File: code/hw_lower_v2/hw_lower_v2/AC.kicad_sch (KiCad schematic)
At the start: 38 parts, among them K1 AHES4191, Q1 BSS138, Q2 BSS138, Q3 BSS138, T1 TS3193-2C 2mA/2mA, U1 BRCS02C, U2 BL0942

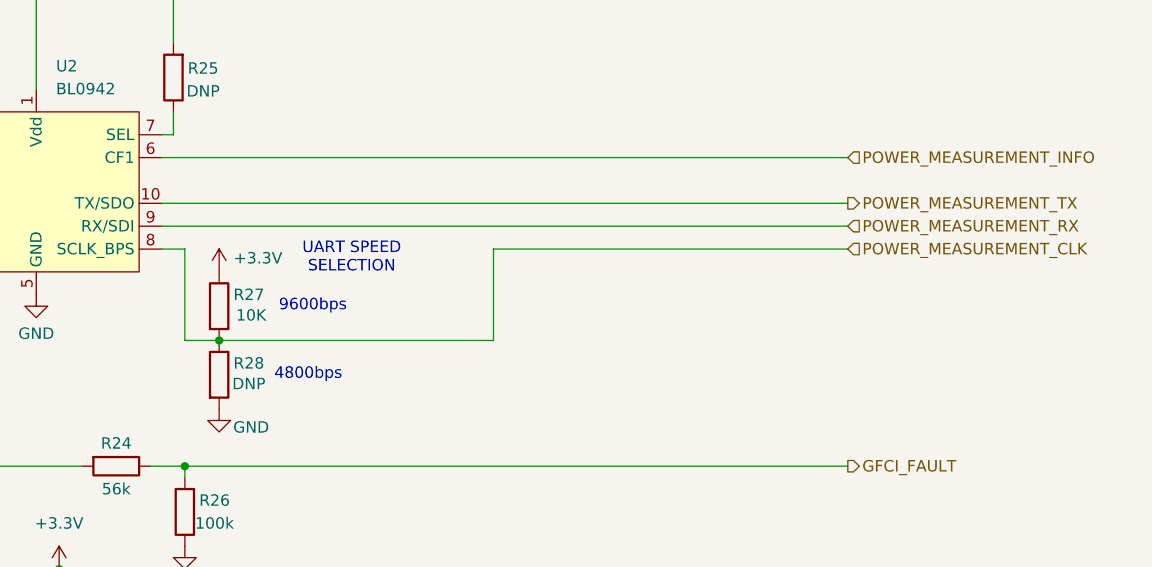
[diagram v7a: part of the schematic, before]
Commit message: grouped and positioned components
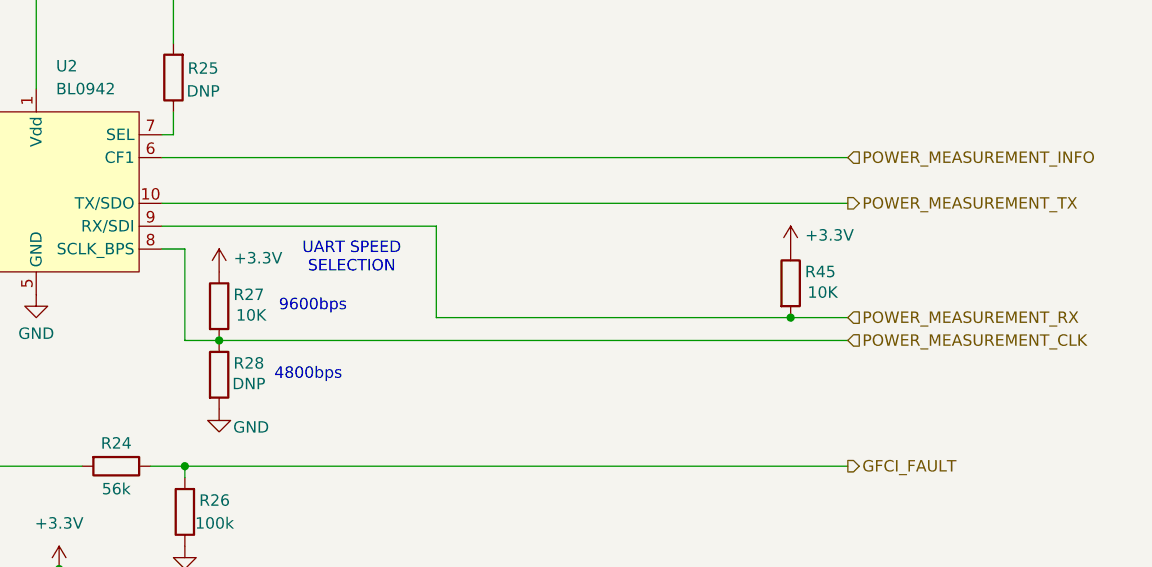
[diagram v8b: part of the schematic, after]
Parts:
- added R45: 10K, Resistor_SMD:R_0603_1608Metric, symbol Device:R
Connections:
- net +3.3V: now also R45.1
- net POWER_MEASUREMENT_RX: now also R45.2
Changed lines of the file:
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@@
 	)
 	(junction
+		(at 240.03 69.85)
+		(diameter 0)
+		(color 0 0 0 0)
+	)
+	(junction
 		(at 97.79 49.53)
 		(diameter 0)
@@
 	(wire
 		(pts
+			(xy 200.66 69.85) (xy 200.66 59.69)
+		)
+		(stroke
+			(width 0)
+			(type default)
+		)
+	)
+	(wire
+		(pts
 			(xy 147.32 33.02) (xy 156.21 33.02)
 		)
@@
 	(wire
 		(pts
-			(xy 170.18 59.69) (xy 246.38 59.69)
+			(xy 240.03 69.85) (xy 246.38 69.85)
+		)
+		(stroke
+			(width 0)
+			(type default)
+		)
+	)
+	(wire
+		(pts
+			(xy 200.66 69.85) (xy 240.03 69.85)
 		)
 		(stroke
@@
 	(wire
 		(pts
-			(xy 207.01 72.39) (xy 207.01 62.23)
+			(xy 109.22 49.53) (xy 146.05 49.53)
 		)
 		(stroke
@@
 	(wire
 		(pts
-			(xy 109.22 49.53) (xy 146.05 49.53)
+			(xy 29.21 77.47) (xy 29.21 83.82)
 		)
 		(stroke
@@
 	(wire
 		(pts
-			(xy 29.21 77.47) (xy 29.21 83.82)
+			(xy 116.84 67.31) (xy 101.6 67.31)
 		)
 		(stroke
@@
 	(wire
 		(pts
-			(xy 116.84 67.31) (xy 101.6 67.31)
+			(xy 200.66 59.69) (xy 170.18 59.69)
 		)
 		(stroke
@@
 	(wire
 		(pts
-			(xy 207.01 62.23) (xy 246.38 62.23)
-		)
-		(stroke
-			(width 0)
-			(type default)
-		)
-	)
-	(wire
-		(pts
 			(xy 101.6 137.16) (xy 107.95 137.16)
 		)
@@
 	(wire
 		(pts
-			(xy 176.53 72.39) (xy 207.01 72.39)
+			(xy 176.53 72.39) (xy 246.38 72.39)
 		)
 		(stroke
@@
 	(hierarchical_label "POWER_MEASUREMENT_RX"
 		(shape input)
-		(at 246.38 59.69 0)
+		(at 246.38 69.85 0)
 		(fields_autoplaced yes)
 		(effects
@@
 	(hierarchical_label "POWER_MEASUREMENT_CLK"
 		(shape input)
-		(at 246.38 62.23 0)
+		(at 246.38 72.39 0)
 		(fields_autoplaced yes)
 		(effects
@@
 	(symbol
 		(lib_id "Device:R")
+		(at 240.03 66.04 0)
+		(unit 1)
+		(exclude_from_sim no)
+		(in_bom yes)
+		(on_board yes)
+		(dnp no)
+		(property "Reference" "R45"
+			(at 243.332 64.77 0)
+			(effects
+				(font
+					(size 1.27 1.27)
+				)
+			)
+		)
+		(property "Value" "10K"
+			(at 243.586 67.056 0)
+			(effects
+				(font
+					(size 1.27 1.27)
+				)
+			)
+		)
+		(property "Footprint" "Resistor_SMD:R_0603_1608Metric"
+			(at 238.252 66.04 90)
+			(effects
+				(font
+					(size 1.27 1.27)
+				)
+				(hide yes)
+			)
+		)
+		(property "Datasheet" "~"
+			(at 240.03 66.04 0)
+			(effects
+				(font
+					(size 1.27 1.27)
+				)
+				(hide yes)
+			)
+		)
+		(property "Description" "Resistor"
+			(at 240.03 66.04 0)
+			(effects
+				(font
+					(size 1.27 1.27)
+				)
+				(hide yes)
+			)
+		)
+		(property "LCSC" "C25804"
+			(at 240.03 66.04 0)
+			(effects
+				(font
+					(size 1.27 1.27)
+				)
+				(hide yes)
+			)
+		)
+		(pin "1"
+		)
+		(pin "2"
+		)
+		(instances
+			(project "hw_lower_v2"
+				(path "/c5175f1c-553a-46da-abbd-483c59ad8dfa/f685e69a-3cdf-4f53-94e9-452320868ecf"
+					(reference "R45")
+					(unit 1)
+				)
+			)
+		)
+	)
+	(symbol
+		(lib_id "Device:R")
 		(at 104.14 49.53 90)
 		(unit 1)
@@
 					(unit 1)
 				)
+			)
+		)
+	)
+	(symbol
+		(lib_id "power:+3.3V")
+		(at 240.03 62.23 0)
+		(unit 1)
+		(exclude_from_sim no)
+		(in_bom yes)
+		(on_board yes)
+		(dnp no)
+		(property "Reference" "#PWR064"
+			(at 240.03 66.04 0)
+			(effects
+				(font
+					(size 1.27 1.27)
+				)
+				(hide yes)
+			)
+		)
+		(property "Value" "+3.3V"
+			(at 244.348 60.706 0)
+			(effects
+				(font
+					(size 1.27 1.27)
+				)
+			)
+		)
+		(property "Footprint" ""
+			(at 240.03 62.23 0)
+			(effects
+				(font
+					(size 1.27 1.27)
+				)
+				(hide yes)
+			)
+		)
+		(property "Datasheet" ""
+			(at 240.03 62.23 0)
+			(effects
+				(font
+					(size 1.27 1.27)
+				)
+				(hide yes)
+			)
+		)
+		(property "Description" "Power symbol creates a global label with name \"+3.3V\""
+			(at 240.03 62.23 0)
+			(effects
+				(font
+					(size 1.27 1.27)
+				)
+				(hide yes)
+			)
+		)
+		(pin "1"
+		)
+		(instances
+			(project "hw_lower_v2"
+				(path "/c5175f1c-553a-46da-abbd-483c59ad8dfa/f685e69a-3cdf-4f53-94e9-452320868ecf"
+					(reference "#PWR064")
+					(unit 1)
+				)
